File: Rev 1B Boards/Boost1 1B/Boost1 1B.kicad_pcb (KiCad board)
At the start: 2 copper layers, 46 x 71.2 mm, 41 parts, among them J18 Banana 2P, J19 Banana 2P, J20 Banana 2P, Q1 BSC059N04LS6, Q2 BSC059N04LS6, Q3 BSC059N04LS6, U1 LM74700, U2 LM5123-Q1

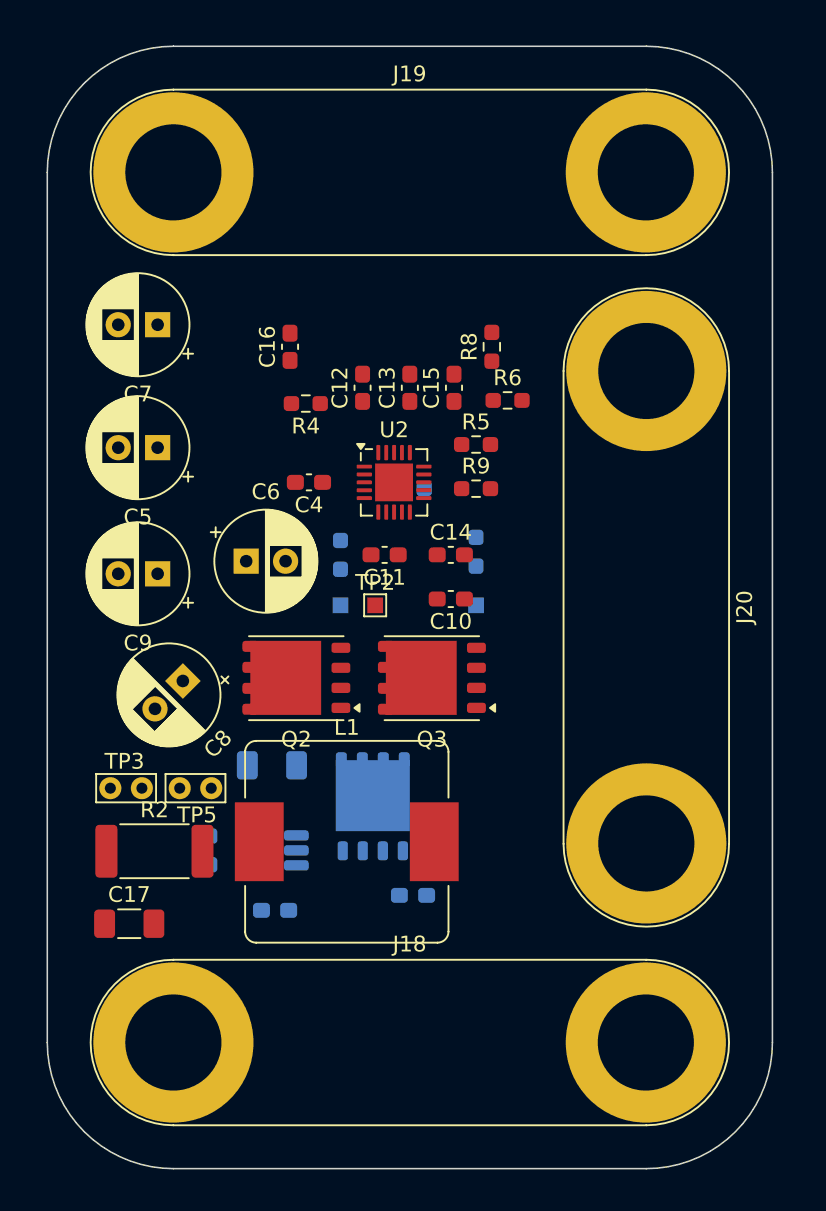
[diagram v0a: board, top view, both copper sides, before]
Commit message: Completed first draft of layout
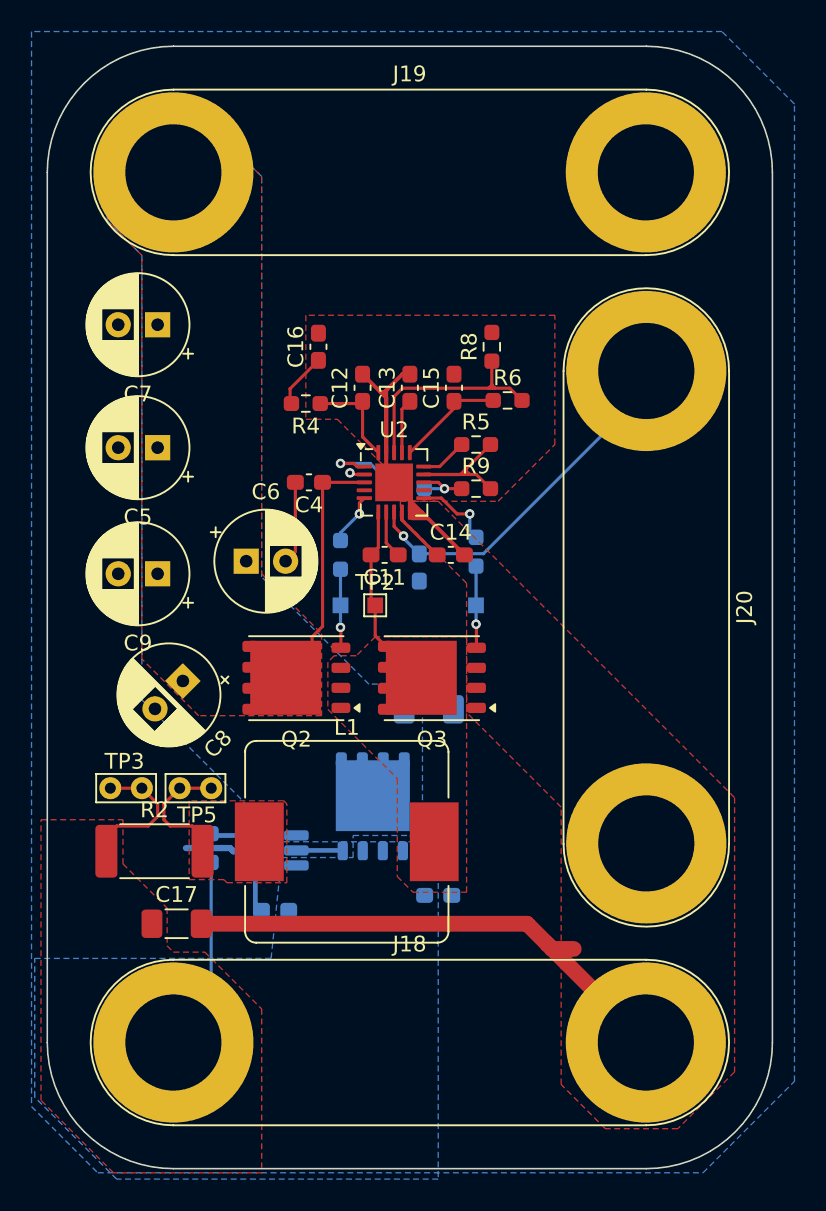
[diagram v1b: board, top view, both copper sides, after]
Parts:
- C10: moved to B.Cu
- moved C2 10.6 mm to (93.2, 158.8), turned to 0 degrees
- moved C17 3.00 mm to (77.2, 172.4)
- moved C10 2.83 mm to (92.6, 149.8), turned to 90 degrees
- moved C16 1.80 mm to (86.2, 135.8)
- moved C1 1.60 mm to (93.8, 170.6)
- moved R10 0.17 mm to (79.4, 167.6)
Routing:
- net GNDPWR: track 0.00 -> 75.9 mm
- net /+6V_{SCAP}_IN: track 0.00 -> 52.9 mm, vias 0 -> 1
- net /Output Boost (Stage 1)/CSN: track 0.00 -> 34.5 mm, vias 0 -> 1
- net +24V: track 0.00 -> 23.3 mm, vias 0 -> 1
- net /+4.4V_{SCAP}_OUT: track 0.00 -> 16.0 mm
- net /Output Boost (Stage 1)/TRK: track 0.00 -> 14.5 mm
- net /Output Boost (Stage 1)/SW: track 0.00 -> 9.10 mm
- net /Output Boost (Stage 1)/VREF: track 0.00 -> 6.92 mm
- net /Output Boost (Stage 1)/COMP: track 0.00 -> 6.41 mm
- net /Output Boost (Stage 1)/LO_R: track 0.00 -> 5.19 mm, vias 0 -> 1
- net /Output Boost (Stage 1)/HO_R: track 0.00 -> 4.99 mm, vias 0 -> 1
- net /Output Boost (Stage 1)/LO: track 0.00 -> 4.98 mm, vias 0 -> 1
- net /Output Boost (Stage 1)/UVLO: track 0.00 -> 3.85 mm, vias 0 -> 1
- net /Output Boost (Stage 1)/VCC: track 0.00 -> 3.66 mm
- net /Output Boost (Stage 1)/COMP_RC: track 0.00 -> 3.52 mm
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- added copper zone on B.Cu, net /+4.4V_{SCAP}_OUT
- added copper zone on F.Cu, net /+4.4V_{SCAP}_OUT
- added copper zone on B.Cu, net /+6V_{SCAP}_IN
- added copper zone on F.Cu, net /+6V_{SCAP}_IN
- added copper zone on F.Cu, net /Output Boost (Stage 1)/CSN
- added copper zone on F.Cu, net /Output Boost (Stage 1)/SW
- added copper zone on B.Cu, net GNDPWR
- added copper zone on F.Cu, net GNDPWR
- added copper zone on In1.Cu, net GNDPWR
- added copper zone on In2.Cu, net GNDPWR
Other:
- copper layers 2 -> 4

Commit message: Adjustments + tons of vias
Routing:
- net GNDPWR: track 75.9 -> 73.1 mm, vias 0 -> 20
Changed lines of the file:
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@@
 		(tags "Infineon OptiMOS")
 		(property "Reference" "Q3"
-			(at 0 -3.9 0)
+			(at -4.4 0 90)
 			(layer "F.SilkS")
 			(effects
@@
 		(tags "CP Radial series Radial pin pitch 2.50mm  diameter 6.3mm Electrolytic Capacitor")
 		(property "Reference" "C7"
-			(at 1.25 -4.4 0)
+			(at 4.2 -3.6 0)
 			(layer "F.SilkS")
 			(effects
@@
 			(at 14.985 -6.24 0)
 			(layer "F.SilkS")
+			(hide yes)
 			(effects
 				(font
@@
 		(tags "capacitor handsolder")
 		(property "Reference" "C4"
-			(at 0 -1.43 0)
+			(at 0 1.4 0)
 			(layer "F.SilkS")
 			(effects
@@
 		(tags "CP Radial series Radial pin pitch 2.50mm  diameter 6.3mm Electrolytic Capacitor")
 		(property "Reference" "C5"
-			(at 1.25 -4.4 0)
+			(at 4.2 -3.8 0)
 			(layer "F.SilkS")
 			(effects
@@
 		(tags "resistor handsolder")
 		(property "Reference" "R6"
-			(at 0 -1.43 0)
+			(at 0.4 -1.4 0)
 			(layer "F.SilkS")
 			(effects
@@
 		(tags "resistor handsolder")
 		(property "Reference" "R2"
-			(at 0 -2.62 0)
+			(at -2.177064 2.8 0)
 			(layer "F.SilkS")
 			(effects
@@
 			(at 1.1 1.7 0)
 			(layer "F.SilkS")
+			(hide yes)
 			(effects
 				(font
@@
 			(at 14.985 -6.24 90)
 			(layer "F.SilkS")
+			(hide yes)
 			(effects
 				(font
@@
 		(tags "CP Radial series Radial pin pitch 2.50mm  diameter 6.3mm Electrolytic Capacitor")
 		(property "Reference" "C6"
-			(at 1.25 -4.4 0)
+			(at -1.817621 -3.4 0)
 			(layer "F.SilkS")
 			(effects
@@
 			(at 1.1 1.7 0)
 			(layer "F.SilkS")
+			(hide yes)
 			(effects
 				(font
@@
 		(tags "Bourns SRP1245A SMD inductor")
 		(property "Reference" "L1"
-			(at 0 -7.25 0)
+			(at 1.2 -7.2 0)
 			(layer "F.SilkS")
 			(effects
@@
 			(at 14.985 -6.24 0)
 			(layer "F.SilkS")
+			(hide yes)
 			(effects
 				(font
@@
 			(at 0 -1.448 0)
 			(layer "F.SilkS")
+			(hide yes)
 			(effects
 				(font
@@
 		(tags "Infineon OptiMOS")
 		(property "Reference" "Q2"
-			(at 0 -3.9 0)
+			(at 4.4 2.2 90)
 			(layer "F.SilkS")
 			(effects
@@
 		(tags "CP Radial series Radial pin pitch 2.50mm  diameter 6.3mm Electrolytic Capacitor")
 		(property "Reference" "C9"
-			(at 1.25 -4.4 0)
+			(at 4.2 -3.8 0)
 			(layer "F.SilkS")
 			(effects
@@
 			(at 0 1.448 180)
 			(layer "B.SilkS")
+			(hide yes)
 			(effects
 				(font
@@
 		(tags "SOT-23-6 Handsoldering")
 		(property "Reference" "U1"
-			(at 0 2.9 0)
+			(at 0.1 -2.55 0)
 			(layer "B.SilkS")
 			(effects
@@
 			(at 0 1.448 180)
 			(layer "B.SilkS")
+			(hide yes)
 			(effects
 				(font
@@
 		(tags "capacitor handsolder")
 		(property "Reference" "C3"
-			(at 0 1.43 0)
+			(at 0.05 -1.65 0)
 			(layer "B.SilkS")
 			(effects
@@
 	)
 	(segment
-		(start 99.435 172.4)
-		(end 100.7175 173.6825)
-		(width 1)
-		(layer "F.Cu")
-		(net 1)
-	)
-	(segment
 		(start 92.75 146.2875)
 		(end 95.4625 149)
@@
 	)
 	(segment
-		(start 78.7625 172.4)
-		(end 99.435 172.4)
-		(width 1)
-		(layer "F.Cu")
-		(net 1)
-	)
-	(segment
 		(start 100.7175 173.6825)
 		(end 106.97 179.935)
@@
 	)
 	(segment
+		(start 81.6 172.4)
+		(end 99.435 172.4)
+		(width 1)
+		(layer "F.Cu")
+		(net 1)
+	)
+	(segment
 		(start 91.525 137.5375)
 		(end 92 137.5375)
@@
 	)
 	(segment
+		(start 99.435 172.4)
+		(end 100.7175 173.6825)
+		(width 1)
+		(layer "F.Cu")
+		(net 1)
+	)
+	(segment
 		(start 90.39375 138.66875)
 		(end 90.5 138.5625)
@@
 		(net 1)
 	)
+	(via
+		(at 98.6 161)
+		(size 0.6)
+		(drill 0.3)
+		(layers "F.Cu" "B.Cu")
+		(free yes)
+		(net 1)
+	)
+	(via
+		(at 98.6 158.6)
+		(size 0.6)
+		(drill 0.3)
+		(layers "F.Cu" "B.Cu")
+		(free yes)
+		(net 1)
+	)
+	(via
+		(at 97.8 155.6)
+		(size 0.6)
+		(drill 0.3)
+		(layers "F.Cu" "B.Cu")
+		(free yes)
+		(net 1)
+	)
+	(via
+		(at 97.8 153.2)
+		(size 0.6)
+		(drill 0.3)
+		(layers "F.Cu" "B.Cu")
+		(free yes)
+		(net 1)
+	)
+	(via
+		(at 98.6 155)
+		(size 0.6)
+		(drill 0.3)
+		(layers "F.Cu" "B.Cu")
+		(free yes)
+		(net 1)
+	)
+	(via
+		(at 98.6 159.8)
+		(size 0.6)
+		(drill 0.3)
+		(layers "F.Cu" "B.Cu")
+		(free yes)
+		(net 1)
+	)
+	(via
+		(at 97.8 154.4)
+		(size 0.6)
+		(drill 0.3)
+		(layers "F.Cu" "B.Cu")
+		(free yes)
+		(net 1)
+	)
+	(via
+		(at 80.8 171.8)
+		(size 0.6)
+		(drill 0.3)
+		(layers "F.Cu" "B.Cu")
+		(net 1)
+	)
+	(via
+		(at 98.6 153.8)
+		(size 0.6)
+		(drill 0.3)
+		(layers "F.Cu" "B.Cu")
+		(free yes)
+		(net 1)
+	)
+	(via
+		(at 98.6 156.2)
+		(size 0.6)
+		(drill 0.3)
+		(layers "F.Cu" "B.Cu")
+		(free yes)
+		(net 1)
+	)
+	(via
+		(at 98.6 157.4)
+		(size 0.6)
+		(drill 0.3)
+		(layers "F.Cu" "B.Cu")
+		(free yes)
+		(net 1)
+	)
+	(via
+		(at 97.8 159.2)
+		(size 0.6)
+		(drill 0.3)
+		(layers "F.Cu" "B.Cu")
+		(free yes)
+		(net 1)
+	)
+	(via
+		(at 80.8 173)
+		(size 0.6)
+		(drill 0.3)
+		(layers "F.Cu" "B.Cu")
+		(net 1)
+	)
+	(via
+		(at 80.2 172.4)
+		(size 0.6)
+		(drill 0.3)
+		(layers "F.Cu" "B.Cu")
+		(net 1)
+	)
+	(via
+		(at 81.6 172.4)
+		(size 0.6)
+		(drill 0.3)
+		(layers "F.Cu" "B.Cu")
+		(net 1)
+	)
+	(via
+		(at 97.8 156.8)
+		(size 0.6)
+		(drill 0.3)
+		(layers "F.Cu" "B.Cu")
+		(free yes)
+		(net 1)
+	)
+	(via
+		(at 98.6 152.6)
+		(size 0.6)
+		(drill 0.3)
+		(layers "F.Cu" "B.Cu")
+		(free yes)
+		(net 1)
+	)
+	(via
+		(at 97.8 158)
+		(size 0.6)
+		(drill 0.3)
+		(layers "F.Cu" "B.Cu")
+		(free yes)
+		(net 1)
+	)
+	(via
+		(at 97.8 160.4)
+		(size 0.6)
+		(drill 0.3)
+		(layers "F.Cu" "B.Cu")
+		(free yes)
+		(net 1)
+	)
+	(via
+		(at 97.8 152)
+		(size 0.6)
+		(drill 0.3)
+		(layers "F.Cu" "B.Cu")
+		(free yes)
+		(net 1)
+	)
 	(segment
 		(start 81.998 167.8)
@@
 			)
 		)
+	)
+	(zone
+		(net 1)
+		(net_name "GNDPWR")
+		(layer "F.Cu")
+		(hatch edge 0.5)
+		(priority 9)
+		(connect_pads yes
+			(clearance 0.5)
+		)
+		(min_thickness 1)
+		(filled_areas_thickness no)
+		(fill yes
+			(thermal_gap 0.5)
+			(thermal_bridge_width 5)
+		)
+		(polygon
+			(pts
+				(xy 78.2 171.4) (xy 78 171.6) (xy 78 173.2) (xy 78.2 173.4) (xy 81.6 173.4) (xy 82.2 172.8) (xy 82.2 172)
+				(xy 81.6 171.4)
+			)
+		)

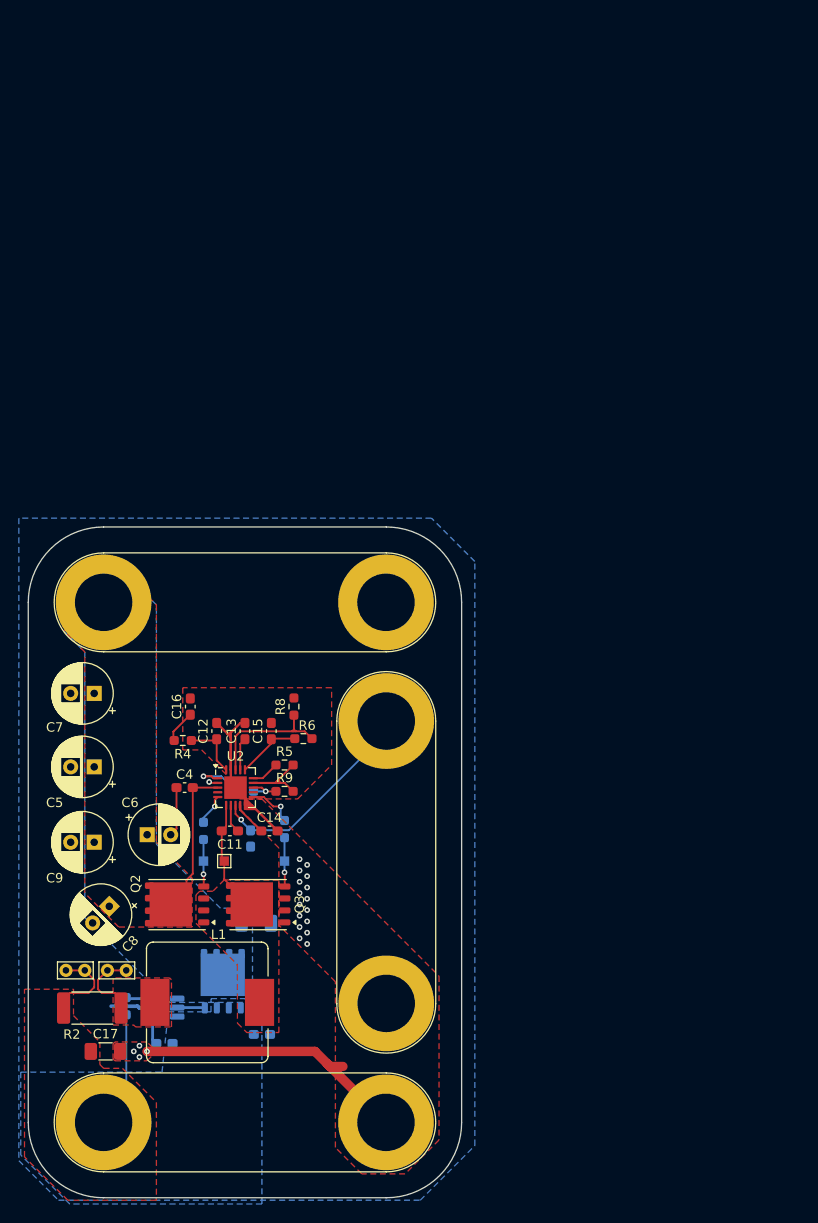
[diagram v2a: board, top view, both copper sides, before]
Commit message: Completed Boost stage 1 layout
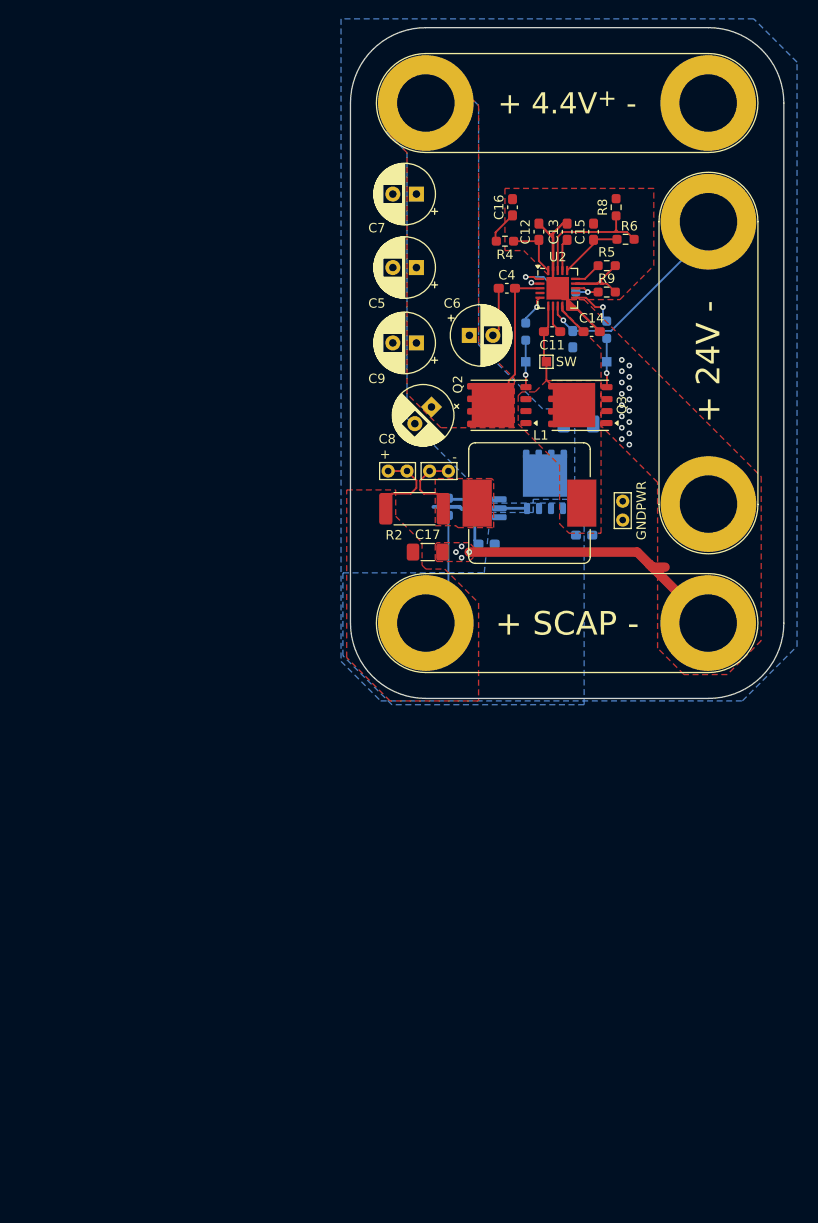
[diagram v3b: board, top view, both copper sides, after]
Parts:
- added G***: LOGO, ! Robomaster Special:StampedeLogo, B.Cu at (126.4, 71.7)
- added TP6: GND, TestPoint:TestPoint_Bridge_Pitch2.0mm_Drill0.7mm, F.Cu at (132.1, 116.0)
- moved C14 63.1 mm to (128.8, 96.0)
- moved C1 63.1 mm to (128.0, 117.6)
- moved C10 63.1 mm to (126.8, 96.8)
- moved C12 63.1 mm to (123.2, 85.4)
- moved C13 63.1 mm to (126.2, 85.4)
- moved C15 63.1 mm to (129.0, 85.4)
- moved C16 63.1 mm to (120.4, 82.8)
- moved C17 63.1 mm to (111.4, 119.4)
- moved C2 63.1 mm to (127.4, 105.8)
- moved C3 63.1 mm to (117.7, 118.5)
- moved C4 63.1 mm to (119.8, 91.4)
- moved C6 63.1 mm to (115.8, 96.4)
- moved C7 63.1 mm to (110.2, 81.4)
- moved C8 63.1 mm to (111.8, 104.0)
- moved J18 63.1 mm to (111.2, 126.9)
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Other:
- board text added: "+"
- board text added: "+ 24V -"
- board text added: "+ 4.4V^{+} -"
- board text added: "+ I_{SENSE} -"
- board text added: "+ SCAP -"
- board text added: "-"
- board text added: "GNDPWR"
- board text added: "HIDRV"
- board text added: "LODRV"
- board text added: "SW"
- board text added: "UT Stampede Supercap Boost (Stage 1) _{Jed Wang}"

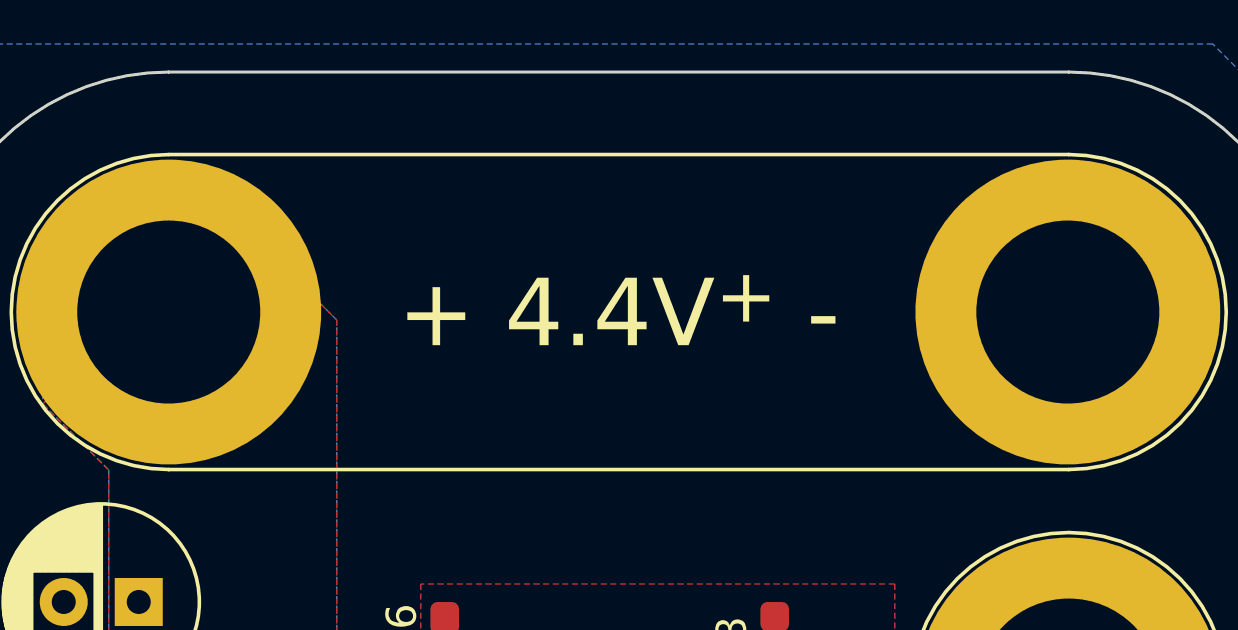
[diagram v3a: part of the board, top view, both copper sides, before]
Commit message: Add dimensions + round corners
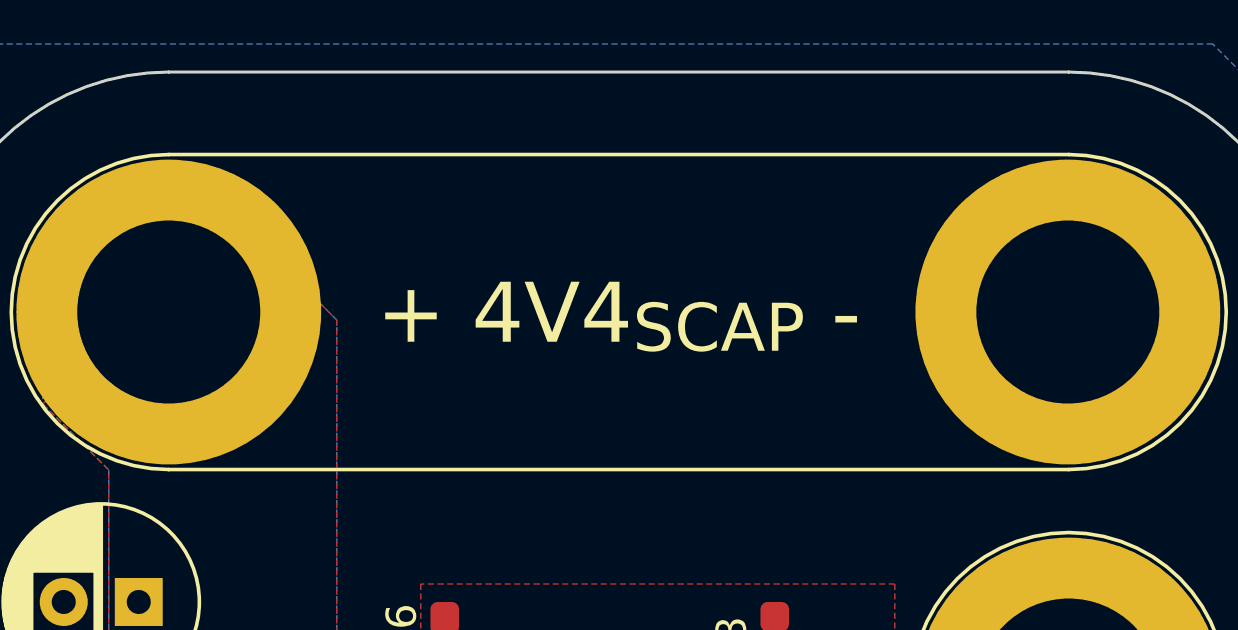
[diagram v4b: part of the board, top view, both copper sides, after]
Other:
- board text added: "+ 4V4_{SCAP} -"
- board text removed: "+ 4.4V^{+} -"
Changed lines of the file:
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@@
 		)
 	)
-	(gr_text "+ 4.4V^{+} -"
+	(gr_text "+ 4V4_{SCAP} -"
 		(at 126.2 71.8 0)
 		(layer "F.SilkS" knockout)
 		(effects
 			(font
-				(size 2.25 2.25)
-				(thickness 0.28125)
+				(size 2 2)
+				(thickness 0.25)
 			)
 		)
@@
 		)
 	)
+	(dimension
+		(type orthogonal)
+		(layer "Dwgs.User")
+		(pts
+			(xy 103.2 126.935) (xy 149.2 126.935)
+		)
+		(height 10.665)
+		(orientation 0)
+		(format
+			(prefix "")
+			(suffix "")
+			(units 3)
+			(units_format 0)
+			(precision 4)
+			(suppress_zeroes yes)
+		)
+		(style
+			(thickness 0.05)
+			(arrow_length 1.27)
+			(text_position_mode 0)
+			(arrow_direction outward)
+			(extension_height 0.58642)
+			(extension_offset 0.5)
+			(keep_text_aligned yes)
+		)
+		(gr_text "46"
+			(at 126.2 136.45 0)
+			(layer "Dwgs.User")
+			(effects
+				(font
+					(size 1 1)
+					(thickness 0.15)
+				)
+			)
+		)
+	)
+	(dimension
+		(type orthogonal)
+		(layer "Dwgs.User")
+		(pts
+			(xy 141.2 134.8) (xy 141.2 63.735)
+		)
+		(height 11.2)
+		(orientation 1)
+		(format
+			(prefix "")
+			(suffix "")
+			(units 3)
+			(units_format 0)
+			(precision 4)
+			(suppress_zeroes yes)
+		)
+		(style
+			(thickness 0.05)
+			(arrow_length 1.27)
+			(text_position_mode 0)
+			(arrow_direction outward)
+			(extension_height 0.58642)
+			(extension_offset 0.5)
+			(keep_text_aligned yes)
+		)
+		(gr_text "71.065"
+			(at 151.25 99.2675 90)
+			(layer "Dwgs.User")
+			(effects
+				(font
+					(size 1 1)
+					(thickness 0.15)
+				)
+			)
+		)
+	)
